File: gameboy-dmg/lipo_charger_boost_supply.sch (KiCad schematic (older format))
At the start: 22 parts, among them J7 USB_B_Micro, U2 TP4056, U3 FS312F-G, U4 FS8205, U5 MT3608

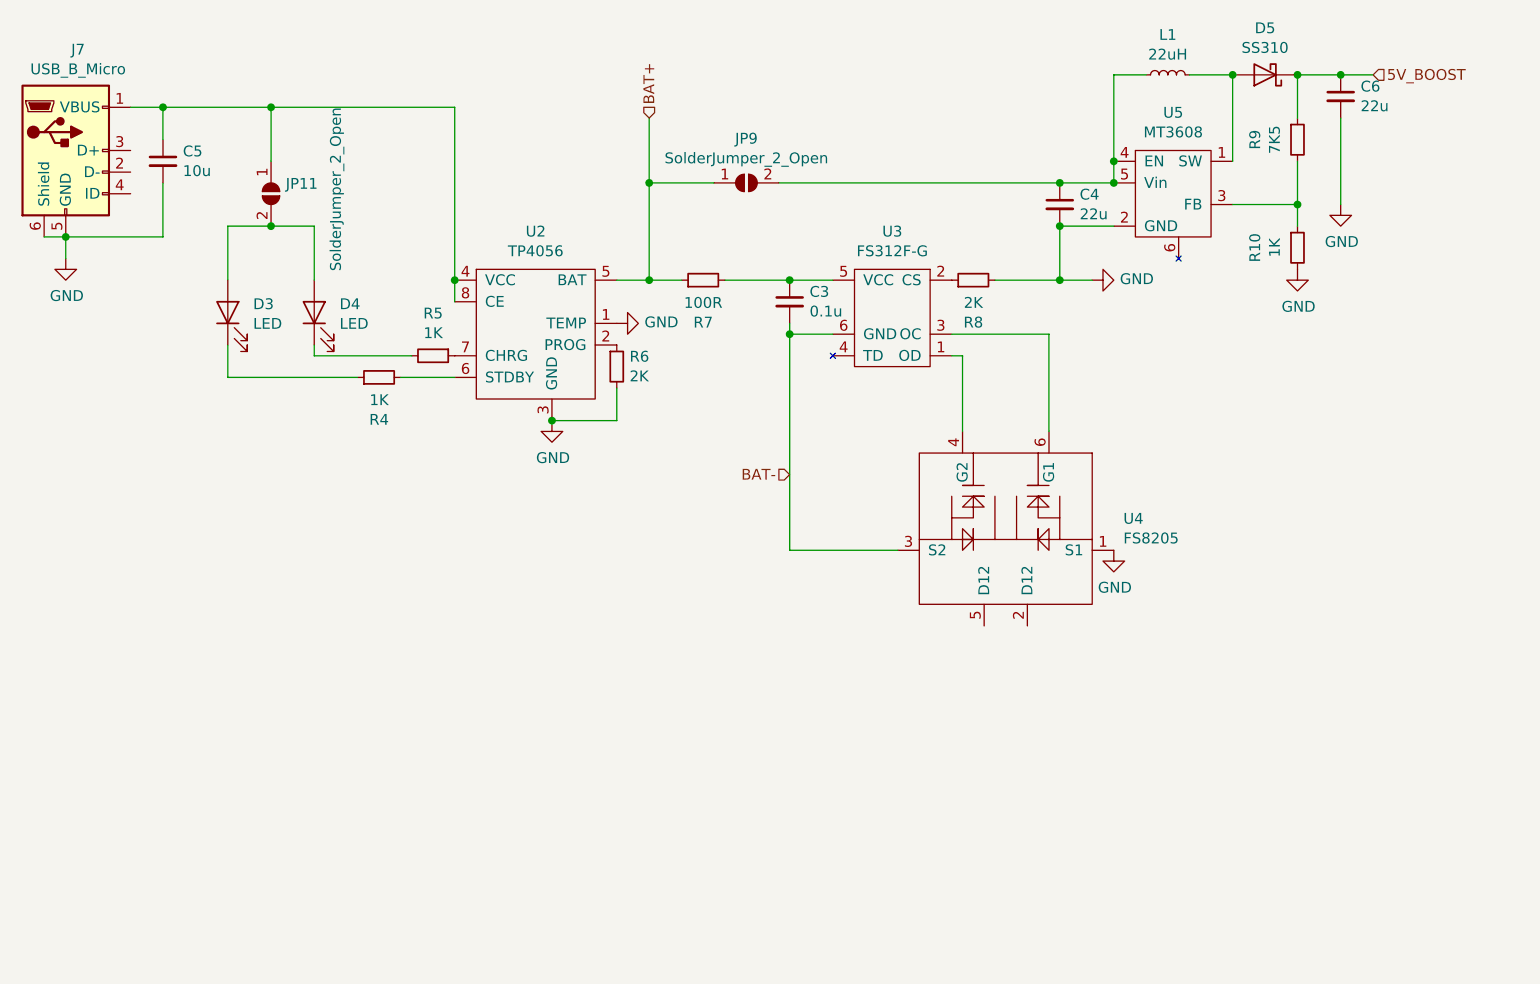
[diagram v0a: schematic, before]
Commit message: Moved buttons and audio to individual sheets and added audio amp
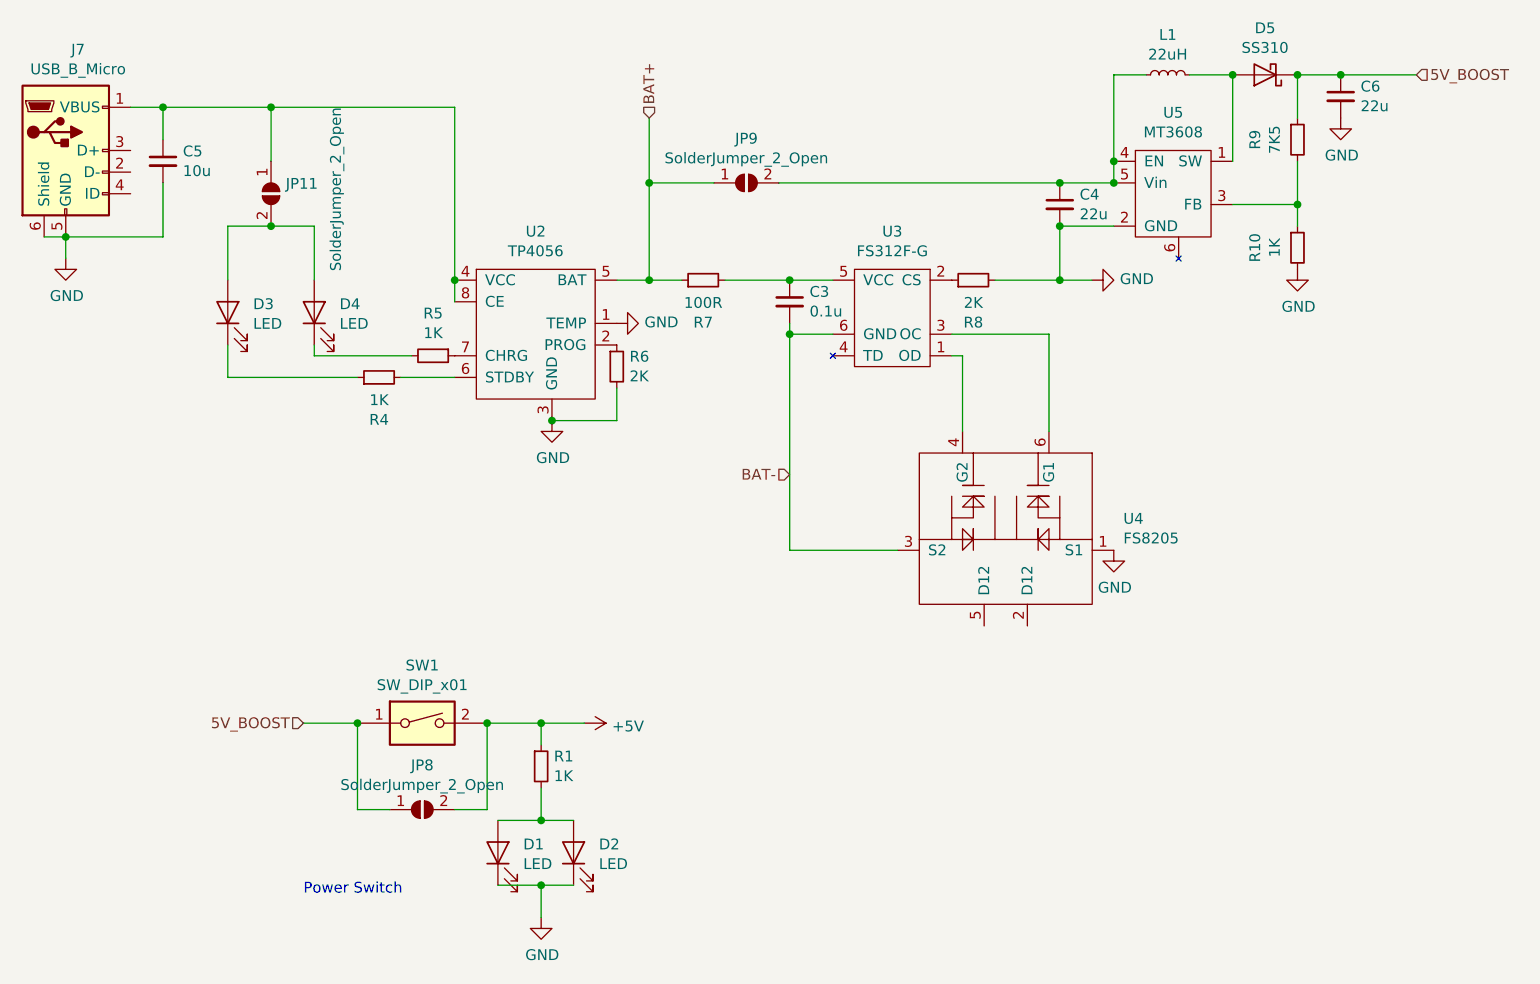
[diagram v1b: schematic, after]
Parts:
- added D1: LED, LED_SMD:LED_0603_1608Metric, symbol Device:LED
- added D2: LED, LED_THT:LED_D3.0mm, symbol Device:LED
- added JP8: SolderJumper_2_Open, Jumper:SolderJumper-2_P1.3mm_Open_RoundedPad1.0x1.5mm, symbol Jumper:SolderJumper_2_Open
- added R1: 1K, Resistor_SMD:R_0603_1608Metric, symbol Device:R_Small
- added SW1: SW_DIP_x01, Connector_PinHeader_2.54mm:PinHeader_1x02_P2.54mm_Vertical, symbol Switch:SW_DIP_x01
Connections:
- net 5V_BOOST: now also JP8.1 (A), SW1.1
- net GND: now also D1.1 (K), D2.1 (K)
- new net: D1.2 (A), D2.2 (A), R1.2
- new net +5V: JP8.2 (B), R1.1, SW1.2
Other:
- note added: "Power Switch"
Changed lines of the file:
@@
 $Descr A4 11693 8268
 encoding utf-8
-Sheet 2 2
+Sheet 2 4
 Title ""
 Date ""
@@
 Wire Wire Line
 	8600 2500 8600 2700
-Text HLabel 8950 2500 2    50   Input ~ 0
+Text HLabel 9150 2500 2    50   Input ~ 0
 5V_BOOST
 Wire Wire Line
-	8950 2500 8800 2500
+	9150 2500 8800 2500
 Connection ~ 8600 2500
 Wire Wire Line
@@
 Wire Wire Line
 	8800 2500 8600 2500
-Wire Wire Line
-	8800 2700 8800 3100
 Connection ~ 6250 3700
 Connection ~ 7500 3000
@@
 L power:GND #PWR0131
 U 1 1 5E8B6045
-P 8800 3100
-F 0 "#PWR0131" H 8800 2850 50  0001 C CNN
-F 1 "GND" H 8805 2927 50  0000 C CNN
-F 2 "" H 8800 3100 50  0001 C CNN
-F 3 "" H 8800 3100 50  0001 C CNN
-	1    8800 3100
-	1    0    0    -1
-$EndComp
+P 8800 2700
+F 0 "#PWR0131" H 8800 2450 50  0001 C CNN
+F 1 "GND" H 8805 2527 50  0000 C CNN
+F 2 "" H 8800 2700 50  0001 C CNN
+F 3 "" H 8800 2700 50  0001 C CNN
+	1    8800 2700
+	1    0    0    -1
+$EndComp
+$Comp
+L Device:R_Small R?
+U 1 1 5E8A7B6E
+P 5100 5700
+AR Path="/5E8A7B6E" Ref="R?"  Part="1"
+AR Path="/5E7FB568/5E8A7B6E" Ref="R1"  Part="1"
+F 0 "R1" H 5159 5746 50  0000 L CNN
+F 1 "1K" H 5159 5655 50  0000 L CNN
+F 2 "Resistor_SMD:R_0603_1608Metric" H 5100 5700 50  0001 C CNN
+F 3 "~" H 5100 5700 50  0001 C CNN
+	1    5100 5700
+	1    0    0    -1
+$EndComp
+$Comp
+L Device:LED D?
+U 1 1 5E8A7B74
+P 4900 6100
+AR Path="/5E8A7B74" Ref="D?"  Part="1"
+AR Path="/5E7FB568/5E8A7B74" Ref="D1"  Part="1"
+F 0 "D1" V 4939 5983 50  0000 R CNN
+F 1 "LED" V 4848 5983 50  0000 R CNN
+F 2 "LED_SMD:LED_0603_1608Metric" H 4900 6100 50  0001 C CNN
+F 3 "~" H 4900 6100 50  0001 C CNN
+	1    4900 6100
+	0    -1   -1   0
+$EndComp
+$Comp
+L Device:LED D?
+U 1 1 5E8A7B7A
+P 5250 6100
+AR Path="/5E8A7B7A" Ref="D?"  Part="1"
+AR Path="/5E7FB568/5E8A7B7A" Ref="D2"  Part="1"
+F 0 "D2" V 5289 5983 50  0000 R CNN
+F 1 "LED" V 5198 5983 50  0000 R CNN
+F 2 "LED_THT:LED_D3.0mm" H 5250 6100 50  0001 C CNN
+F 3 "~" H 5250 6100 50  0001 C CNN
+	1    5250 6100
+	0    -1   -1   0
+$EndComp
+Wire Wire Line
+	4900 5950 5100 5950
+$Comp
+L power:GND #PWR?
+U 1 1 5E8A7B81
+P 5100 6400
+AR Path="/5E8A7B81" Ref="#PWR?"  Part="1"
+AR Path="/5E7FB568/5E8A7B81" Ref="#PWR0101"  Part="1"
+F 0 "#PWR0101" H 5100 6150 50  0001 C CNN
+F 1 "GND" H 5105 6227 50  0000 C CNN
+F 2 "" H 5100 6400 50  0001 C CNN
+F 3 "" H 5100 6400 50  0001 C CNN
+	1    5100 6400
+	1    0    0    -1
+$EndComp
+Wire Wire Line
+	4900 6250 5100 6250
+Wire Wire Line
+	5100 6250 5100 6400
+Wire Wire Line
+	5100 6250 5250 6250
+Connection ~ 5100 6250
+Wire Wire Line
+	5100 5800 5100 5950
+Connection ~ 5100 5950
+Wire Wire Line
+	5100 5950 5250 5950
+$Comp
+L Switch:SW_DIP_x01 SW?
+U 1 1 5E8A7B8E
+P 4550 5500
+AR Path="/5E8A7B8E" Ref="SW?"  Part="1"
+AR Path="/5E7FB568/5E8A7B8E" Ref="SW1"  Part="1"
+F 0 "SW1" H 4550 5767 50  0000 C CNN
+F 1 "SW_DIP_x01" H 4550 5676 50  0000 C CNN
+F 2 "Connector_PinHeader_2.54mm:PinHeader_1x02_P2.54mm_Vertical" H 4550 5500 50  0001 C CNN
+F 3 "~" H 4550 5500 50  0001 C CNN
+	1    4550 5500
+	1    0    0    -1
+$EndComp
+$Comp
+L power:+5V #PWR?
+U 1 1 5E8A7B94
+P 5300 5500
+AR Path="/5E8A7B94" Ref="#PWR?"  Part="1"
+AR Path="/5E7FB568/5E8A7B94" Ref="#PWR0102"  Part="1"
+F 0 "#PWR0102" H 5300 5350 50  0001 C CNN
+F 1 "+5V" V 5315 5628 50  0000 L CNN
+F 2 "" H 5300 5500 50  0001 C CNN
+F 3 "" H 5300 5500 50  0001 C CNN
+	1    5300 5500
+	0    1    1    0
+$EndComp
+$Comp
+L Jumper:SolderJumper_2_Open JP?
+U 1 1 5E8A7B9A
+P 4550 5900
+AR Path="/5E8A7B9A" Ref="JP?"  Part="1"
+AR Path="/5E7FB568/5E8A7B9A" Ref="JP8"  Part="1"
+F 0 "JP8" H 4550 6105 50  0000 C CNN
+F 1 "SolderJumper_2_Open" H 4550 6014 50  0000 C CNN
+F 2 "Jumper:SolderJumper-2_P1.3mm_Open_RoundedPad1.0x1.5mm" H 4550 5900 50  0001 C CNN
+F 3 "~" H 4550 5900 50  0001 C CNN
+	1    4550 5900
+	1    0    0    -1
+$EndComp
+Wire Wire Line
+	4250 5500 4250 5900
+Wire Wire Line
+	4250 5900 4400 5900
+Wire Wire Line
+	4700 5900 4850 5900
+Wire Wire Line
+	4850 5900 4850 5500
+Wire Wire Line
+	4850 5500 5100 5500
+Connection ~ 4850 5500
+Wire Wire Line
+	5100 5600 5100 5500
+Connection ~ 5100 5500
+Wire Wire Line
+	5100 5500 5300 5500
+Wire Wire Line
+	4000 5500 4250 5500
+Connection ~ 4250 5500
+Text HLabel 4000 5500 0    50   Input ~ 0
+5V_BOOST
+Text Notes 4000 6300 0    50   ~ 0
+Power Switch
 $EndSCHEMATC
